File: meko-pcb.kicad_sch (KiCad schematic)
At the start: 7 parts, among them IC1 ES9218PQ, IC2 AS5600-ASOM, J1 FH34SRJ-24S-0.5SH_99_, J2 Micro_SD_Card, SW1 SW_Push, U1 ESP32-MINI-1, U2 CP2102N-Axx-xQFN28

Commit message: worked on power a lil bit
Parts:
- removed U2: CP2102N-Axx-xQFN28, Package_DFN_QFN:QFN-28-1EP_5x5mm_P0.5mm_EP3.35x3.35mm, symbol Interface_USB:CP2102N-Axx-xQFN28
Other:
- added sheet USB (usb.kicad_sch)
- added sheet power (power.kicad_sch)
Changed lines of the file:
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@@
 	(paper "A4")
-	(symbol
-		(lib_id "Interface_USB:CP2102N-Axx-xQFN28")
-		(at 273.05 93.98 0)
-		(unit 1)
-		(exclude_from_sim no)
-		(in_bom yes)
-		(on_board yes)
-		(dnp no)
-		(fields_autoplaced yes)
-		(property "Reference" "U2"
-			(at 275.1933 127 0)
-			(effects
-				(font
-					(size 1.27 1.27)
-				)
-				(justify left)
-			)
-		)
-		(property "Value" "CP2102N-Axx-xQFN28"
-			(at 275.1933 129.54 0)
-			(effects
-				(font
-					(size 1.27 1.27)
-				)
-				(justify left)
-			)
-		)
-		(property "Footprint" "Package_DFN_QFN:QFN-28-1EP_5x5mm_P0.5mm_EP3.35x3.35mm"
-			(at 306.07 125.73 0)
-			(effects
-				(font
-					(size 1.27 1.27)
-				)
-				(hide yes)
-			)
-		)
-		(property "Datasheet" "https://www.silabs.com/documents/public/data-sheets/cp2102n-datasheet.pdf"
-			(at 274.32 113.03 0)
-			(effects
-				(font
-					(size 1.27 1.27)
-				)
-				(hide yes)
-			)
-		)
-		(property "Description" "USB to UART master bridge, QFN-28"
-			(at 273.05 93.98 0)
-			(effects
-				(font
-					(size 1.27 1.27)
-				)
-				(hide yes)
-			)
-		)
-		(pin "21"
-		)
-		(pin "2"
-		)
-		(pin "3"
-		)
-		(pin "15"
-		)
-		(pin "27"
-		)
-		(pin "29"
-		)
-		(pin "1"
-		)
-		(pin "12"
-		)
-		(pin "17"
-		)
-		(pin "26"
-		)
-		(pin "14"
-		)
-		(pin "24"
-		)
-		(pin "19"
-		)
-		(pin "28"
-		)
-		(pin "11"
-		)
-		(pin "8"
-		)
-		(pin "20"
-		)
-		(pin "25"
-		)
-		(pin "16"
-		)
-		(pin "9"
-		)
-		(pin "6"
-		)
-		(pin "13"
-		)
-		(pin "5"
-		)
-		(pin "22"
-		)
-		(pin "4"
-		)
-		(pin "10"
-		)
-		(pin "23"
-		)
-		(pin "7"
-		)
-		(pin "18"
-		)
-		(instances
-			(project ""
-				(path "/bdd43acd-23c1-472b-909a-8e24eb60d56d"
-					(reference "U2")
-					(unit 1)
-				)
-			)
-		)
-	)
 	(symbol
 		(lib_id "FH34SRJ-24S-0_5SH_99_:FH34SRJ-24S-0.5SH_99_")
@@
 				)
 			)
+		)
+	)
+	(sheet
+		(at 31.75 21.59)
+		(size 24.13 14.605)
+		(exclude_from_sim no)
+		(in_bom yes)
+		(on_board yes)
+		(dnp no)
+		(fields_autoplaced yes)
+		(stroke
+			(width 0.1524)
+			(type solid)
+		)
+		(fill
+			(color 0 0 0 0.0000)
+		)
+		(property "Sheetname" "power"
+			(at 31.75 20.8784 0)
+			(effects
+				(font
+					(size 1.27 1.27)
+				)
+				(justify left bottom)
+			)
+		)
+		(property "Sheetfile" "power.kicad_sch"
+			(at 31.75 36.7796 0)
+			(effects
+				(font
+					(size 1.27 1.27)
+				)
+				(justify left top)
+			)
+		)
+		(instances
+			(project "meko-pcb"
+				(path "/bdd43acd-23c1-472b-909a-8e24eb60d56d"
+					(page "2")
+				)
+			)
+		)
+	)
+	(sheet
+		(at 168.275 22.86)
+		(size 33.02 22.86)
+		(exclude_from_sim no)
+		(in_bom yes)
+		(on_board yes)
+		(dnp no)
+		(fields_autoplaced yes)
+		(stroke
+			(width 0.1524)
+			(type solid)
+		)
+		(fill
+			(color 0 0 0 0.0000)
+		)
+		(property "Sheetname" "USB"
+			(at 168.275 22.1484 0)
+			(effects
+				(font
+					(size 1.27 1.27)
+				)
+				(justify left bottom)
+			)
+		)
+		(property "Sheetfile" "usb.kicad_sch"
+			(at 168.275 46.3046 0)
+			(effects
+				(font
+					(size 1.27 1.27)
+				)
+				(justify left top)
+			)
+		)
+		(instances
+			(project "meko-pcb"
+				(path "/bdd43acd-23c1-472b-909a-8e24eb60d56d"
+					(page "3")
+				)
+			)

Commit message: did power and usb
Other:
- sheet USB ports: added CTS, RSTb, RTS, RXD, SUSP, SUSPb, TXD; removed none
- sheet power ports: added EN2; removed none
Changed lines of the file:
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@@
 	(generator_version "9.0")
 	(paper "A4")
+	(wire
+		(pts
+			(xy 191.77 38.1) (xy 191.77 50.8)
+		)
+		(stroke
+			(width 0)
+			(type default)
+		)
+	)
+	(wire
+		(pts
+			(xy 187.96 38.1) (xy 191.77 38.1)
+		)
+		(stroke
+			(width 0)
+			(type default)
+		)
+	)
+	(wire
+		(pts
+			(xy 187.96 50.8) (xy 191.77 50.8)
+		)
+		(stroke
+			(width 0)
+			(type default)
+		)
+	)
 	(symbol
 		(lib_id "FH34SRJ-24S-0_5SH_99_:FH34SRJ-24S-0.5SH_99_")
@@
 	)
 	(sheet
-		(at 31.75 21.59)
-		(size 24.13 14.605)
+		(at 174.625 47.625)
+		(size 13.335 5.08)
 		(exclude_from_sim no)
 		(in_bom yes)
@@
 		)
 		(property "Sheetname" "power"
-			(at 31.75 20.8784 0)
+			(at 174.625 46.9134 0)
 			(effects
 				(font
@@
 		)
 		(property "Sheetfile" "power.kicad_sch"
-			(at 31.75 36.7796 0)
-			(effects
-				(font
-					(size 1.27 1.27)
-				)
-				(justify left top)
+			(at 174.625 53.2896 0)
+			(effects
+				(font
+					(size 1.27 1.27)
+				)
+				(justify left top)
+			)
+		)
+		(pin "EN2" input
+			(at 187.96 50.8 0)
+			(effects
+				(font
+					(size 1.27 1.27)
+				)
+				(justify right)
 			)
 		)
@@
 	)
 	(sheet
-		(at 168.275 22.86)
-		(size 33.02 22.86)
+		(at 168.275 26.035)
+		(size 19.685 16.51)
 		(exclude_from_sim no)
 		(in_bom yes)
@@
 		)
 		(property "Sheetname" "USB"
-			(at 168.275 22.1484 0)
+			(at 168.275 25.3234 0)
 			(effects
 				(font
@@
 		)
 		(property "Sheetfile" "usb.kicad_sch"
-			(at 168.275 46.3046 0)
-			(effects
-				(font
-					(size 1.27 1.27)
-				)
-				(justify left top)
-			)
-		)
+			(at 168.275 43.1296 0)
+			(effects
+				(font
+					(size 1.27 1.27)
+				)
+				(justify left top)
+			)
+		)
+		(pin "CTS" output
+			(at 168.275 33.02 180)
+			(effects
+				(font
+					(size 1.27 1.27)
+				)
+				(justify left)
+			)
+		)
+		(pin "RSTb" output
+			(at 187.96 30.48 0)
+			(effects
+				(font
+					(size 1.27 1.27)
+				)
+				(justify right)
+			)
+		)
+		(pin "RTS" output
+			(at 168.275 30.48 180)
+			(effects
+				(font
+					(size 1.27 1.27)
+				)
+				(justify left)
+			)
+		)
+		(pin "RXD" output
+			(at 168.275 38.1 180)
+			(effects
+				(font
+					(size 1.27 1.27)
+				)
+				(justify left)
+			)
+		)
+		(pin "SUSP" output
+			(at 187.96 38.1 0)
+			(effects
+				(font
+					(size 1.27 1.27)
+				)
+				(justify right)
+			)
+		)
+		(pin "SUSPb" output
+			(at 187.96 40.64 0)
+			(effects
+				(font
+					(size 1.27 1.27)
+				)
+				(justify right)
+			)
+		)
+		(pin "TXD" input
+			(at 168.275 40.64 180)
+			(effects
+				(font
+					(size 1.27 1.27)
+				)
+				(justify left)
+			)
+		)

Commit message: did work on the audio
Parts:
- removed IC1: ES9218PQ, ES9218PQ:QFN40P500X500X80-41N-D, symbol ES9218PQ:ES9218PQ
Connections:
- net GND: now reaches U1.1 (GND), U1.2 (GND), U1.27 (GND), U1.38 (GND), U1.39 (GND), U1.40 (GND), U1.41 (GND), U1.42 (GND), U1.43 (GND), U1.44 (GND), U1.45 (GND), U1.46 (GND), U1.47 (GND), U1.48 (GND), U1.49 (GND), U1.50 (GND), U1.51 (GND), U1.52 (GND), U1.53 (GND), U1.54 (GND), U1.55 (GND)
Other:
- added sheet audio (audio.kicad_sch)
- moved on the sheet: IC2, J1, J2

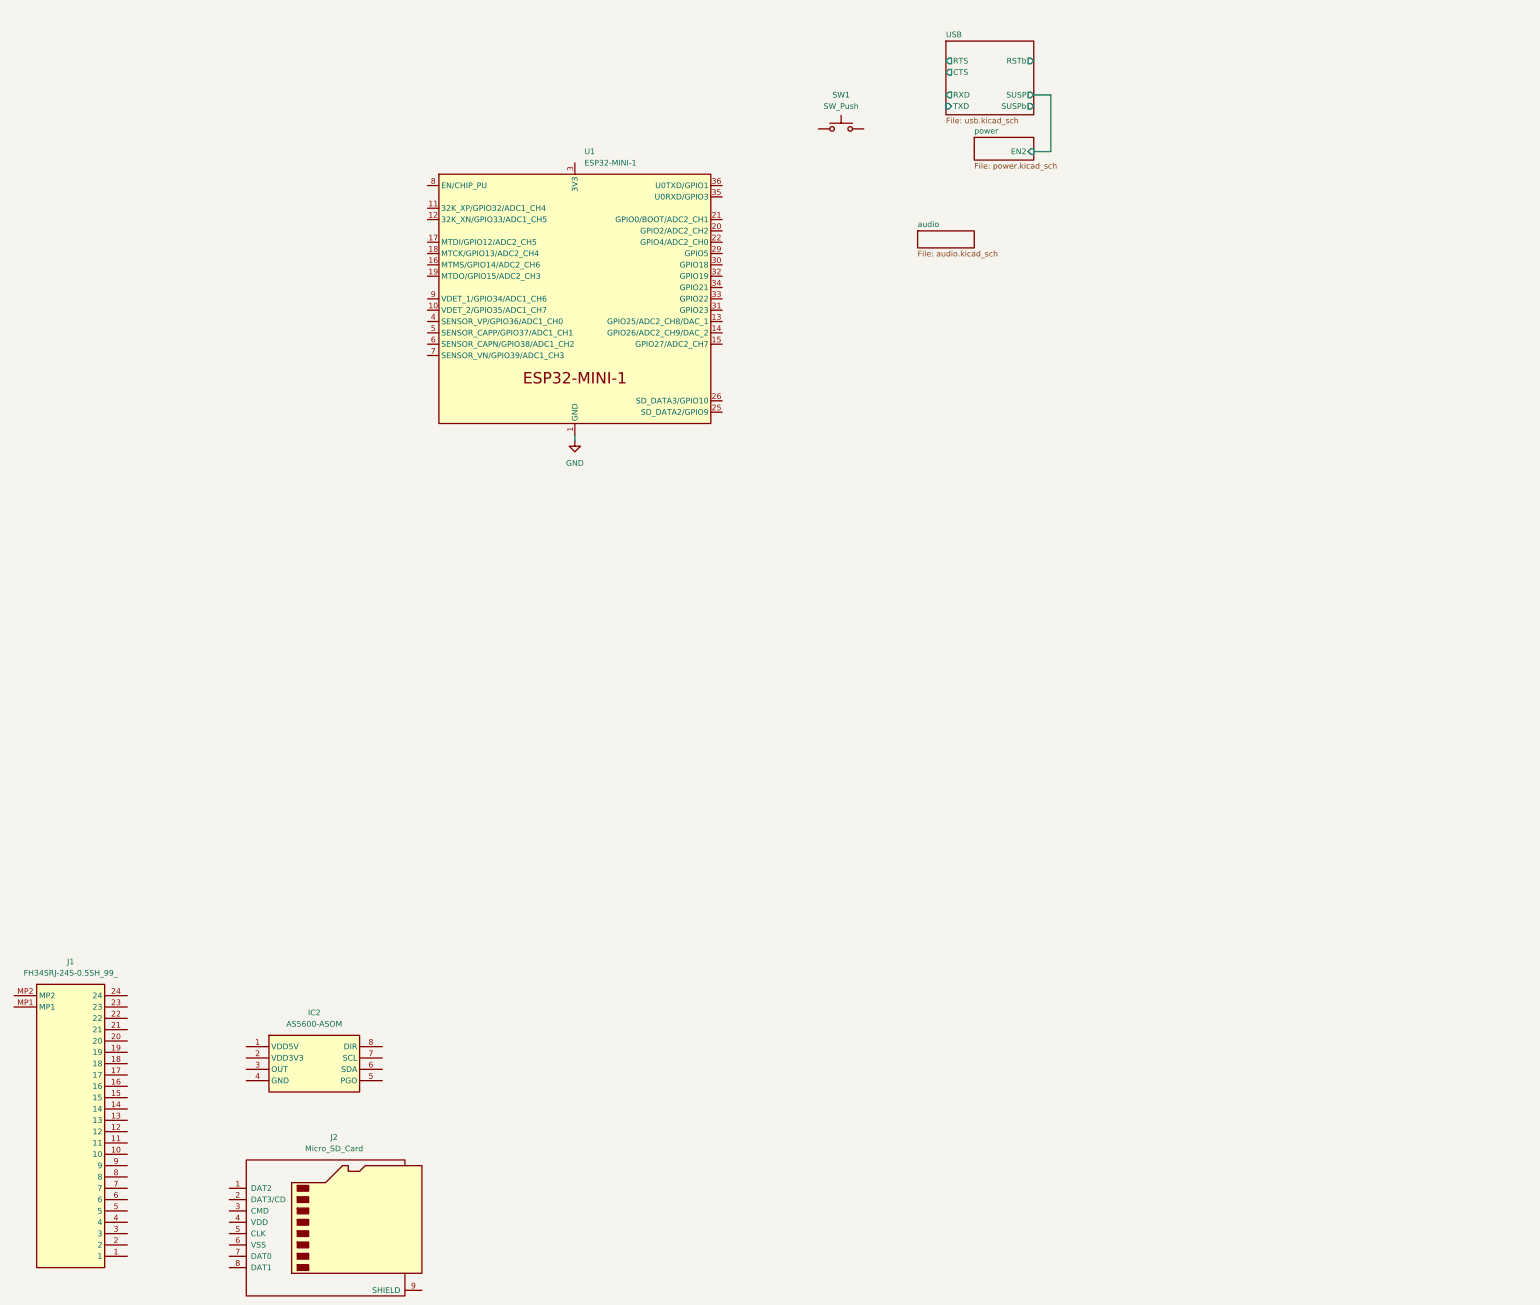
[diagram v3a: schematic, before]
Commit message: changed the crystal for an oscillator, still dont know what to do wit XO pin
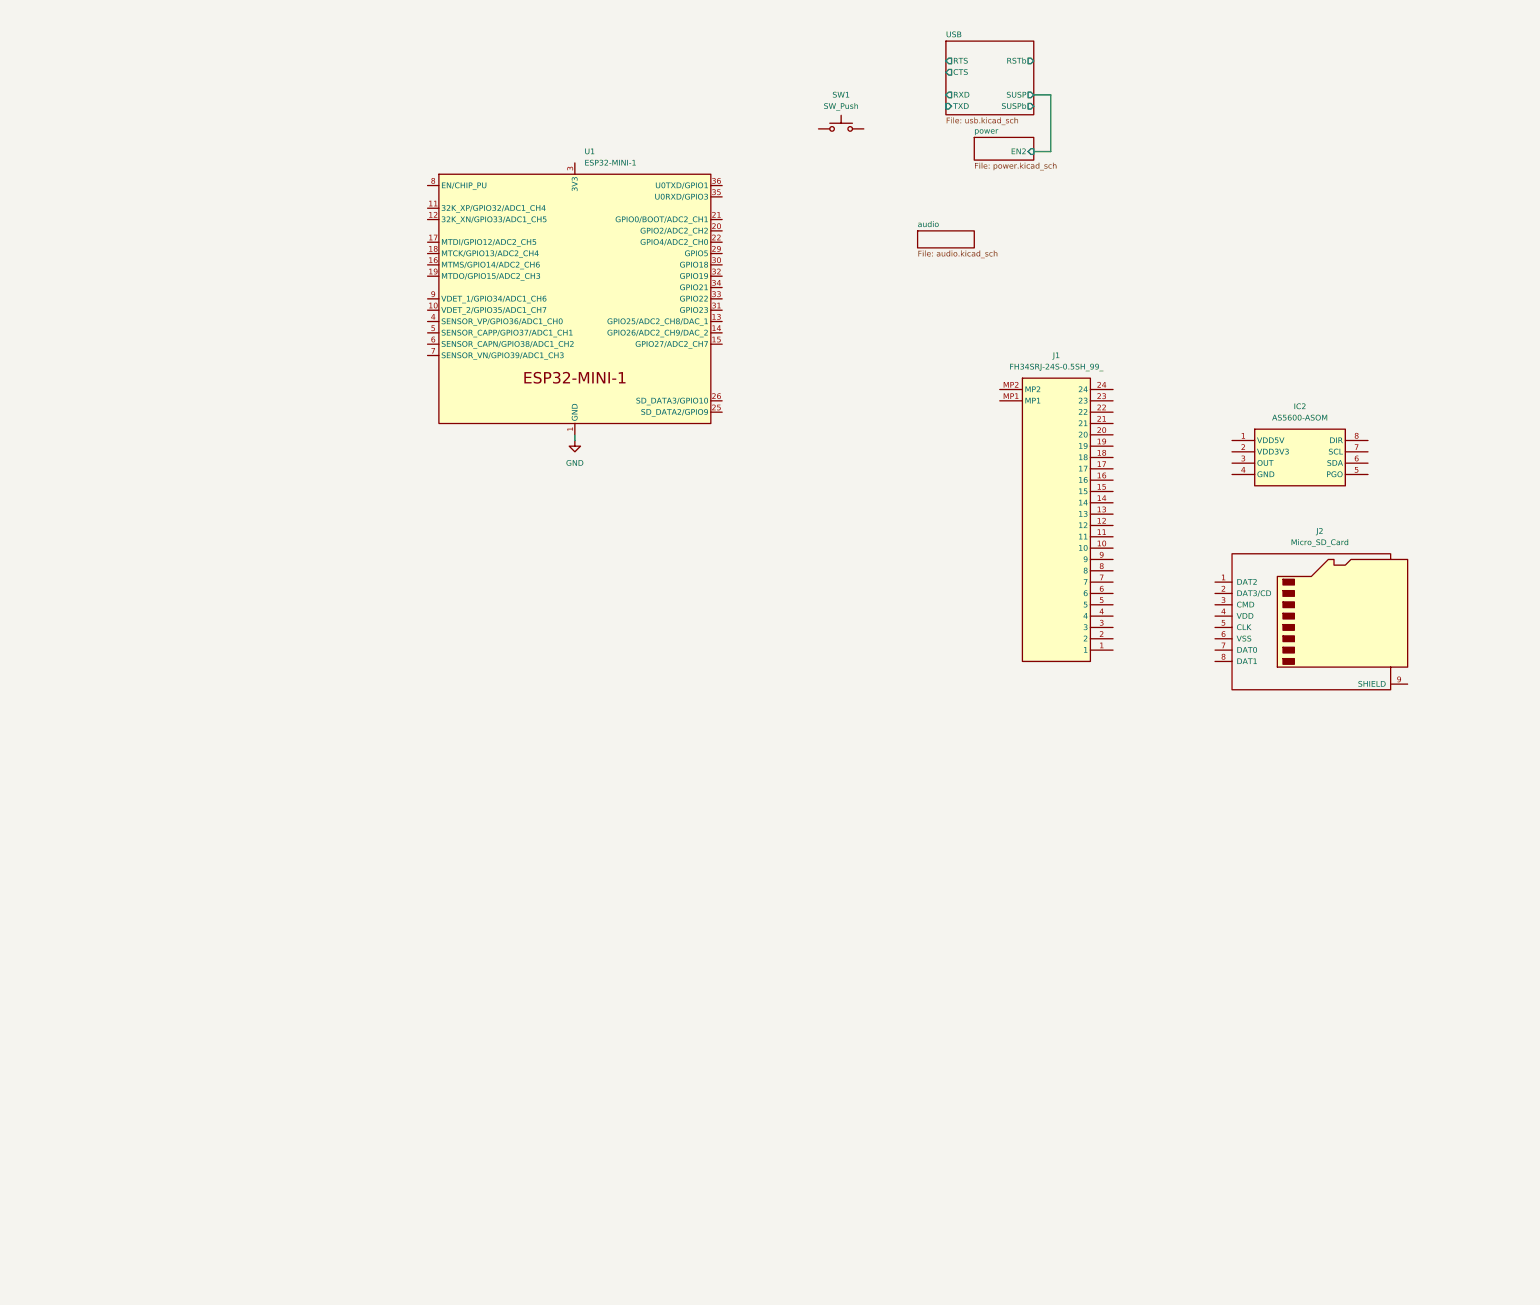
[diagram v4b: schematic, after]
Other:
- moved on the sheet: IC2, J1, J2
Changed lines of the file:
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@@
 	(symbol
 		(lib_id "FH34SRJ-24S-0_5SH_99_:FH34SRJ-24S-0.5SH_99_")
-		(at -40.64 240.03 0)
+		(at 180.34 104.14 0)
 		(unit 1)
 		(exclude_from_sim no)
@@
 		(fields_autoplaced yes)
 		(property "Reference" "J1"
-			(at -27.94 232.41 0)
+			(at 193.04 96.52 0)
 			(effects
 				(font
@@
 		)
 		(property "Value" "FH34SRJ-24S-0.5SH_99_"
-			(at -27.94 234.95 0)
+			(at 193.04 99.06 0)
 			(effects
 				(font
@@
 		)
 		(property "Footprint" "FH34SRJ24S05SH99"
-			(at -19.05 334.95 0)
+			(at 201.93 199.06 0)
 			(effects
 				(font
@@
 		)
 		(property "Datasheet" "https://www.hirose.com/en/product/document?clcode=CL0580-1255-6-99&productname=FH34SRJ-24S-0.5SH(99)&series=FH34SRJ&documenttype=2DDrawing&lang=en&documentid=0000990903"
-			(at -19.05 434.95 0)
+			(at 201.93 299.06 0)
 			(effects
 				(font
@@
 		)
 		(property "Description" "24 Position FFC, FPC Connector Contacts, Top and Bottom 0.020\" (0.50mm) Surface Mount, Right Angle"
-			(at -40.64 240.03 0)
+			(at 180.34 104.14 0)
 			(effects
 				(font
@@
 		)
 		(property "Height" "1.1"
-			(at -19.05 634.95 0)
+			(at 201.93 499.06 0)
 			(effects
 				(font
@@
 		)
 		(property "Manufacturer_Name" "Hirose"
-			(at -19.05 734.95 0)
+			(at 201.93 599.06 0)
 			(effects
 				(font
@@
 		)
 		(property "Manufacturer_Part_Number" "FH34SRJ-24S-0.5SH(99)"
-			(at -19.05 834.95 0)
+			(at 201.93 699.06 0)
 			(effects
 				(font
@@
 		)
 		(property "Mouser Part Number" "798-FH34SRJ24S05SH99"
-			(at -19.05 934.95 0)
+			(at 201.93 799.06 0)
 			(effects
 				(font
@@
 		)
 		(property "Mouser Price/Stock" "https://www.mouser.co.uk/ProductDetail/Hirose-Connector/FH34SRJ-24S-0.5SH99?qs=vcbW%252B4%252BSTIpKBl5ap9J8Fw%3D%3D"
-			(at -19.05 1034.95 0)
+			(at 201.93 899.06 0)
 			(effects
 				(font
@@
 		)
 		(property "Arrow Part Number" ""
-			(at -19.05 1134.95 0)
+			(at 201.93 999.06 0)
 			(effects
 				(font
@@
 		)
 		(property "Arrow Price/Stock" ""
-			(at -19.05 1234.95 0)
+			(at 201.93 1099.06 0)
 			(effects
 				(font
@@
 	(symbol
 		(lib_id "Connector:Micro_SD_Card")
-		(at 30.48 290.83 0)
+		(at 251.46 154.94 0)
 		(unit 1)
 		(exclude_from_sim no)
@@
 		(fields_autoplaced yes)
 		(property "Reference" "J2"
-			(at 31.115 271.78 0)
+			(at 252.095 135.89 0)
 			(effects
 				(font
@@
 		)
 		(property "Value" "Micro_SD_Card"
-			(at 31.115 274.32 0)
+			(at 252.095 138.43 0)
 			(effects
 				(font
@@
 		)
 		(property "Footprint" "Connector_Card:microSD_HC_Molex_47219-2001"
-			(at 59.69 283.21 0)
+			(at 280.67 147.32 0)
 			(effects
 				(font
@@
 		)
 		(property "Datasheet" "https://www.we-online.com/components/products/datasheet/693072010801.pdf"
-			(at 30.48 290.83 0)
+			(at 251.46 154.94 0)
 			(effects
 				(font
@@
 		)
 		(property "Description" "Micro SD Card Socket"
-			(at 30.48 290.83 0)
+			(at 251.46 154.94 0)
 			(effects
 				(font
@@
 	(symbol
 		(lib_id "AS5600-ASOM:AS5600-ASOM")
-		(at 11.43 251.46 0)
+		(at 232.41 115.57 0)
 		(unit 1)
 		(exclude_from_sim no)
@@
 		(fields_autoplaced yes)
 		(property "Reference" "IC2"
-			(at 26.67 243.84 0)
+			(at 247.65 107.95 0)
 			(effects
 				(font
@@
 		)
 		(property "Value" "AS5600-ASOM"
-			(at 26.67 246.38 0)
+			(at 247.65 110.49 0)
 			(effects
 				(font
@@
 		)
 		(property "Footprint" "SOIC127P600X175-8N"
-			(at 38.1 346.38 0)
+			(at 259.08 210.49 0)
 			(effects
 				(font
@@
 		)
 		(property "Datasheet" "https://datasheet.datasheetarchive.com/originals/distributors/DKDS-11/214624.pdf"
-			(at 38.1 446.38 0)
+			(at 259.08 310.49 0)
 			(effects
 				(font
@@
 		)
 		(property "Description" "IC SENSOR MAG ROTARY 12BIT 8SOIC"
-			(at 11.43 251.46 0)
+			(at 232.41 115.57 0)
 			(effects
 				(font
@@
 		)
 		(property "Height" "1.75"
-			(at 38.1 646.38 0)
+			(at 259.08 510.49 0)
 			(effects
 				(font
@@
 		)
 		(property "Manufacturer_Name" "ams OSRAM"
-			(at 38.1 746.38 0)
+			(at 259.08 610.49 0)
 			(effects
 				(font
@@
 		)
 		(property "Manufacturer_Part_Number" "AS5600-ASOM"
-			(at 38.1 846.38 0)
+			(at 259.08 710.49 0)
 			(effects
 				(font
@@
 		)
 		(property "Mouser Part Number" "985-AS5600-ASOM"
-			(at 38.1 946.38 0)
+			(at 259.08 810.49 0)
 			(effects
 				(font
@@
 		)
 		(property "Mouser Price/Stock" "https://www.mouser.co.uk/ProductDetail/ams-OSRAM/AS5600-ASOM?qs=KTMMzrZdriG6aU1h9lJCUQ%3D%3D"
-			(at 38.1 1046.38 0)
+			(at 259.08 910.49 0)
 			(effects
 				(font
@@
 		)
 		(property "Arrow Part Number" "AS5600-ASOM"
-			(at 38.1 1146.38 0)
+			(at 259.08 1010.49 0)
 			(effects
 				(font
@@
 		)
 		(property "Arrow Price/Stock" "https://www.arrow.com/en/products/as5600-asom/ams-osram?utm_currency=USD&region=nac"
-			(at 38.1 1246.38 0)
-			(effects
-				(font
+			(at 259.08 1110.49 0)
+			(effects
+				(font
